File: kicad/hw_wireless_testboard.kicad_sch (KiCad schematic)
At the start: 0 parts

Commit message: minor changes
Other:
- added sheet LORA (LORA.kicad_sch)
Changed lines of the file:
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@@
+		)
+	)
+	(sheet
+		(at 33.02 81.28)
+		(size 63.5 35.56)
+		(fields_autoplaced yes)
+		(stroke
+			(width 0.1524)
+			(type solid)
+		)
+		(fill
+			(color 0 0 0 0.0000)
+		)
+		(property "Sheetname" "LORA"
+			(at 33.02 80.5684 0)
+			(effects
+				(font
+					(size 1.27 1.27)
+				)
+				(justify left bottom)
+			)
+		)
+		(property "Sheetfile" "LORA.kicad_sch"
+			(at 33.02 117.4246 0)
+			(effects
+				(font
+					(size 1.27 1.27)
+				)
+				(justify left top)
+			)
+		)
+		(instances
+			(project "hw_wireless_testboard"
+				(path "/601a88ea-2da7-4ec4-b637-f587eb4ba821"
+					(page "3")
+				)
+			)
 		)
 	)

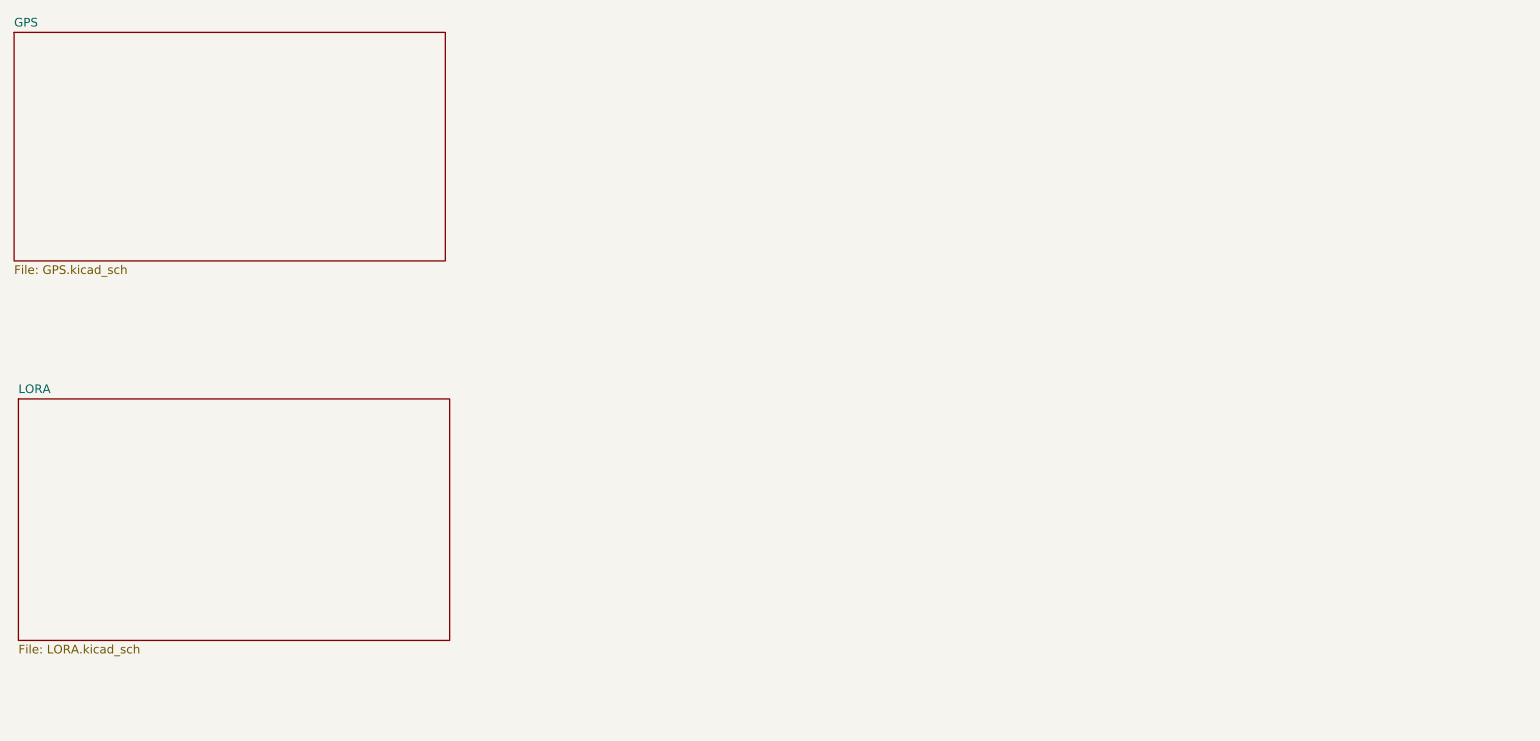
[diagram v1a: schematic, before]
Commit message: [kicad] fixed grid size, added oscillator |  to LoRa chip, added BLE and WiFi chip [resources] Added info relating to additions on kicad
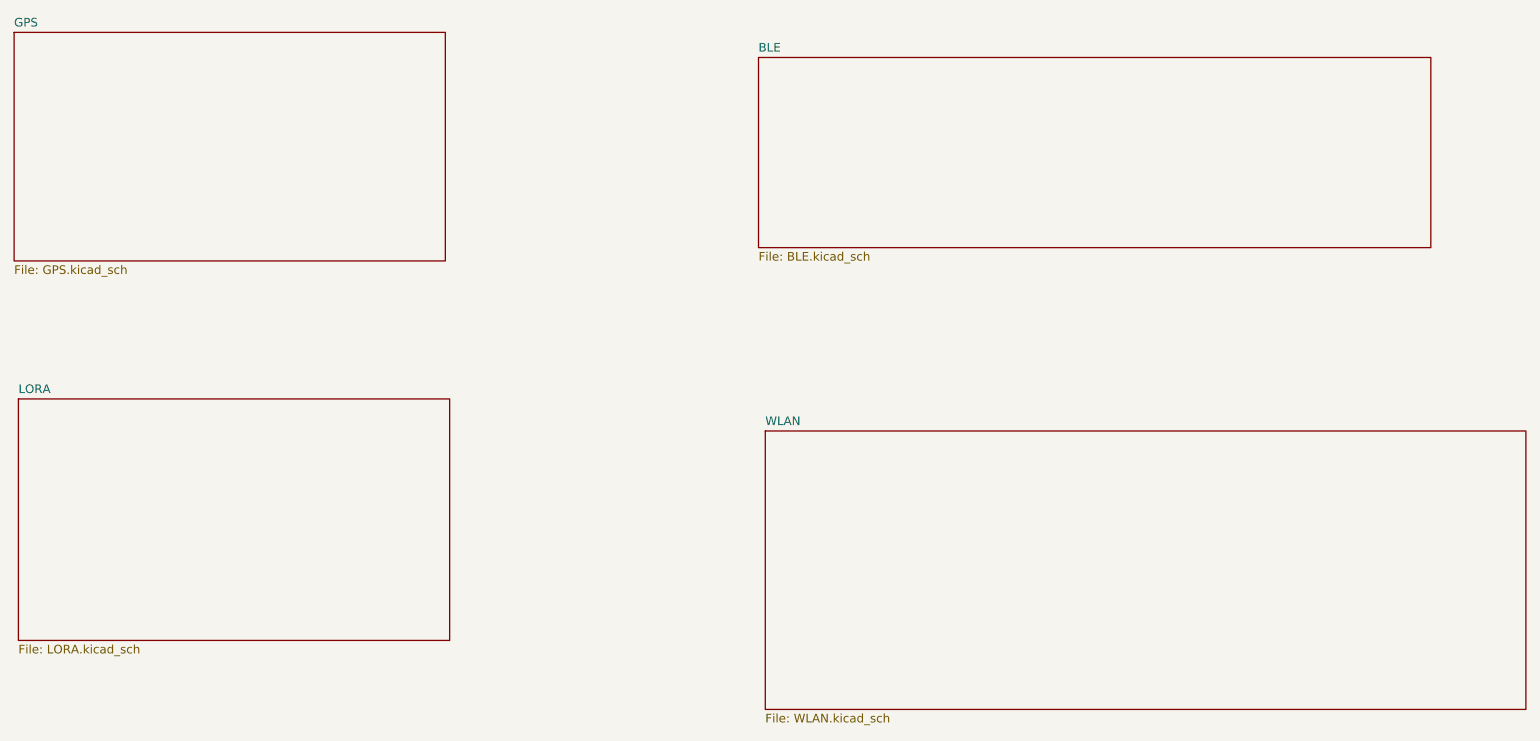
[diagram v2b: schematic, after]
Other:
- added sheet BLE (BLE.kicad_sch)
- added sheet WLAN (WLAN.kicad_sch)
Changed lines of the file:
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@@
 	(paper "A4")
+	(sheet
+		(at 142 31)
+		(size 99 28)
+		(fields_autoplaced yes)
+		(stroke
+			(width 0.1524)
+			(type solid)
+		)
+		(fill
+			(color 0 0 0 0.0000)
+		)
+		(property "Sheetname" "BLE"
+			(at 142 30.2884 0)
+			(effects
+				(font
+					(size 1.27 1.27)
+				)
+				(justify left bottom)
+			)
+		)
+		(property "Sheetfile" "BLE.kicad_sch"
+			(at 142 59.5846 0)
+			(effects
+				(font
+					(size 1.27 1.27)
+				)
+				(justify left top)
+			)
+		)
+		(instances
+			(project "hw_wireless_testboard"
+				(path "/601a88ea-2da7-4ec4-b637-f587eb4ba821"
+					(page "4")
+				)
+			)
+		)
+	)
 	(sheet
 		(at 32.385 27.305)
@@
 				)
 			)
+		)
+	)
+	(sheet
+		(at 143 86)
+		(size 112 41)
+		(fields_autoplaced yes)
+		(stroke
+			(width 0.1524)
+			(type solid)
+		)
+		(fill
+			(color 0 0 0 0.0000)
+		)
+		(property "Sheetname" "WLAN"
+			(at 143 85.2884 0)
+			(effects
+				(font
+					(size 1.27 1.27)
+				)
+				(justify left bottom)
+			)
+		)
+		(property "Sheetfile" "WLAN.kicad_sch"
+			(at 143 127.5846 0)
+			(effects
+				(font
+					(size 1.27 1.27)
+				)
+				(justify left top)
+			)
+		)
+		(property "Field2" ""
+			(at 143 86 0)
+			(effects
+				(font
+					(size 1.27 1.27)
+				)
+				(hide yes)
+			)
+		)
+		(instances
+			(project "hw_wireless_testboard"
+				(path "/601a88ea-2da7-4ec4-b637-f587eb4ba821"
+					(page "5")
+				)
+			)

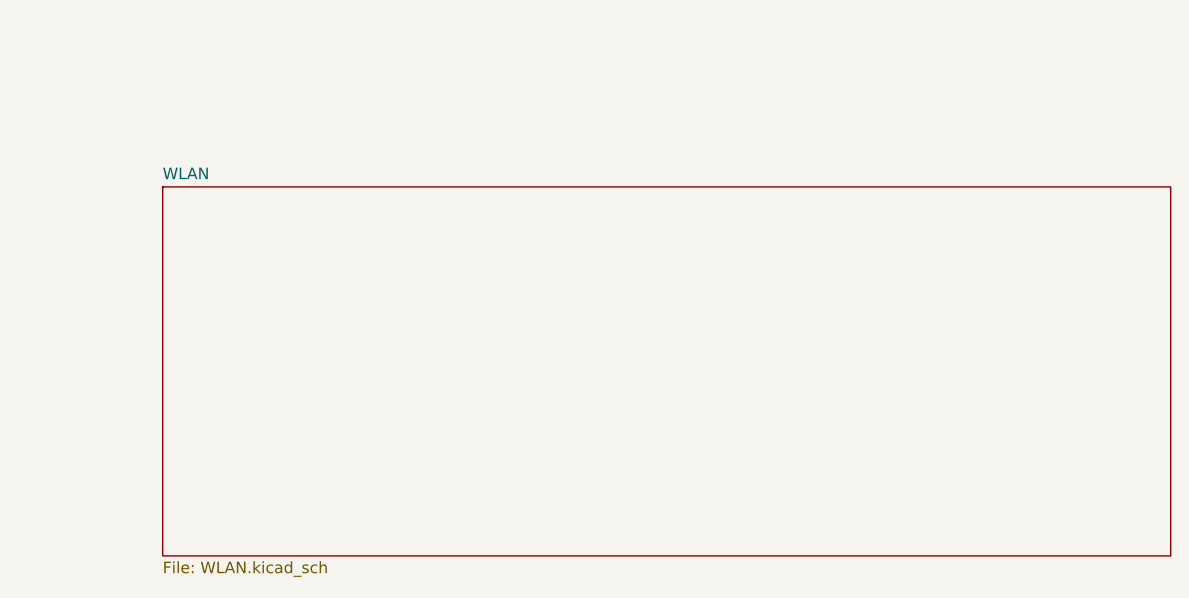
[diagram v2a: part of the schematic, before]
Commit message: finished bluetooth schematic apart from anteantenna-design, WiFi design started
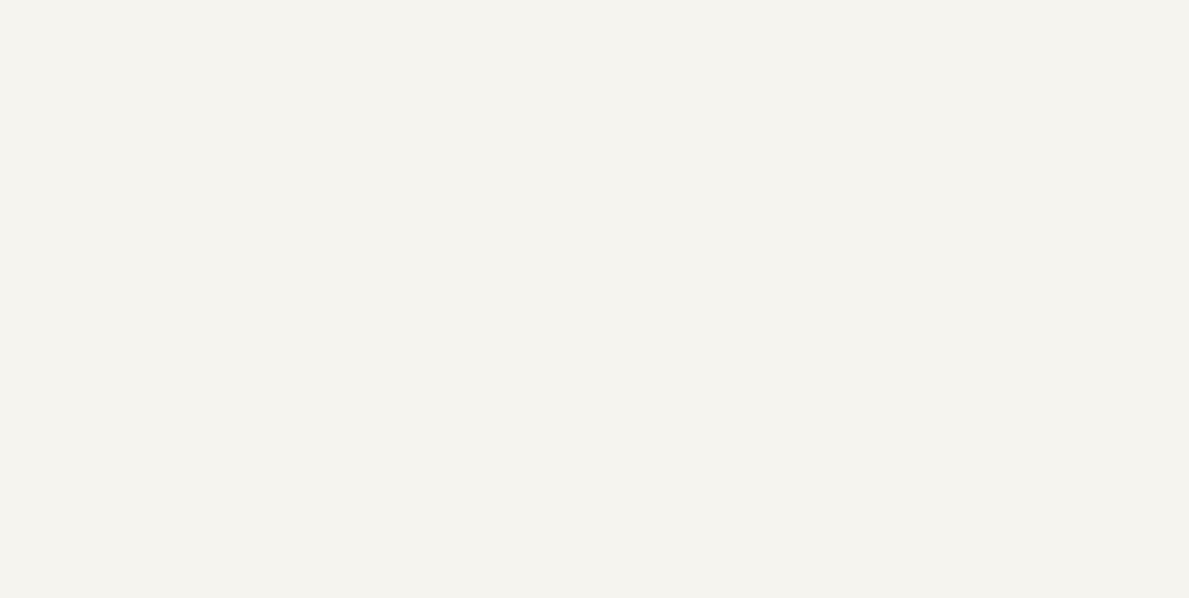
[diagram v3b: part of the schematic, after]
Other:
- removed sheet WLAN
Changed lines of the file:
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@@
-		)
-	)
-	(sheet
-		(at 143 86)
-		(size 112 41)
-		(fields_autoplaced yes)
-		(stroke
-			(width 0.1524)
-			(type solid)
-		)
-		(fill
-			(color 0 0 0 0.0000)
-		)
-		(property "Sheetname" "WLAN"
-			(at 143 85.2884 0)
-			(effects
-				(font
-					(size 1.27 1.27)
-				)
-				(justify left bottom)
-			)
-		)
-		(property "Sheetfile" "WLAN.kicad_sch"
-			(at 143 127.5846 0)
-			(effects
-				(font
-					(size 1.27 1.27)
-				)
-				(justify left top)
-			)
-		)
-		(property "Field2" ""
-			(at 143 86 0)
-			(effects
-				(font
-					(size 1.27 1.27)
-				)
-				(hide yes)
-			)
-		)
-		(instances
-			(project "hw_wireless_testboard"
-				(path "/601a88ea-2da7-4ec4-b637-f587eb4ba821"
-					(page "5")
-				)
-			)
 		)
 	)
